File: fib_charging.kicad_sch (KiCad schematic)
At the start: 42 parts, among them J301 Conn_01x02, J302 Conn_01x02, J303 Conn_01x02, Q301 CSD17581Q3A, Q302 CSD17581Q3A, Q303 CSD17581Q3A, Q304 CSD17581Q3A, U301 BQ25798RQMR

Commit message: partially implemented E-INK PMIC
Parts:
- added R1, R2: 0R, Resistor_SMD:R_0603_1608Metric, symbol Device:R_Small
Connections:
- net USBPD1_HV: now also R1.2
- net USBPD2_HV: now also R2.2
- net VBUS_CHG: now also R1.1, R2.1
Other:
- note removed: "Can i just connect USBPD_HV-s together?"

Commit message: did a ton of routing and modeling for SOM, USB, DP & Charging/Power, things starting to take shape
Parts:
- J301, J302, J303: footprint Connector_JST:JST_EH_S2B-EH_1x02_P2.50mm_Horizontal -> Connector_JST:JST_PH_S2B-PH-SM4-TB_1x02-1MP_P2.00mm_Horizontal
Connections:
- net GND: now also J301.2 (Pin_2), J303.1 (Pin_1); no longer J301.1 (Pin_1), J303.2 (Pin_2)
- net CHG_VBUS: now reaches C303.1, C304.1, C307.1, Q303.5 (D), Q304.5 (D), U301.2 (VBUS), U301.3 (VBUS)
- net VBUS_SOLAR: now reaches C301.1, Q301.5 (D), U301.8 (VAC2)
- net VBUS_SOLAR: now also J301.1 (Pin_1); no longer J301.2 (Pin_2)
- net at C311.1, C314.1, R306.1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: now also J302.2 (Pin_2); no longer J302.1 (Pin_1)
- net VBUS_CHG renamed VBUS_USB
- new net: J302.1 (Pin_1), J303.2 (Pin_2)
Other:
- moved on the sheet: J301, J302, J303
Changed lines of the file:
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@@
 	(wire
 		(pts
-			(xy 222.25 104.14) (xy 227.33 104.14)
+			(xy 224.79 46.99) (xy 222.25 46.99)
 		)
 		(stroke
@@
 	(wire
 		(pts
-			(xy 199.39 91.44) (xy 199.39 93.98)
+			(xy 222.25 104.14) (xy 227.33 104.14)
 		)
 		(stroke
@@
 	(wire
 		(pts
-			(xy 120.65 55.88) (xy 130.81 55.88)
+			(xy 199.39 91.44) (xy 199.39 93.98)
 		)
 		(stroke
@@
 	(wire
 		(pts
-			(xy 81.28 82.55) (xy 87.63 82.55)
+			(xy 120.65 55.88) (xy 130.81 55.88)
 		)
 		(stroke
@@
 	(wire
 		(pts
-			(xy 224.79 60.96) (xy 224.79 64.77)
+			(xy 81.28 82.55) (xy 87.63 82.55)
 		)
 		(stroke
@@
 	(wire
 		(pts
+			(xy 45.72 68.58) (xy 48.26 68.58)
+		)
+		(stroke
+			(width 0)
+			(type default)
+		)
+	)
+	(wire
+		(pts
 			(xy 209.55 63.5) (xy 209.55 64.77)
 		)
@@
 	(wire
 		(pts
-			(xy 124.46 96.52) (xy 127 96.52)
+			(xy 222.25 46.99) (xy 222.25 52.07)
 		)
 		(stroke
@@
 	(wire
 		(pts
-			(xy 223.52 67.31) (xy 224.79 67.31)
+			(xy 124.46 96.52) (xy 127 96.52)
 		)
 		(stroke
@@
 	(wire
 		(pts
-			(xy 45.72 68.58) (xy 48.26 68.58)
+			(xy 45.72 66.04) (xy 53.34 66.04)
 		)
 		(stroke
@@
 	(wire
 		(pts
-			(xy 45.72 66.04) (xy 53.34 66.04)
+			(xy 187.96 90.17) (xy 187.96 91.44)
 		)
 		(stroke
@@
 	(wire
 		(pts
-			(xy 187.96 90.17) (xy 187.96 91.44)
+			(xy 189.23 58.42) (xy 189.23 60.96)
 		)
 		(stroke
@@
 	(wire
 		(pts
-			(xy 189.23 58.42) (xy 189.23 60.96)
+			(xy 87.63 63.5) (xy 102.87 63.5)
 		)
 		(stroke
@@
 	(wire
 		(pts
-			(xy 87.63 63.5) (xy 102.87 63.5)
+			(xy 224.79 49.53) (xy 224.79 55.88)
 		)
 		(stroke
@@
 		)
 	)
+	(label "VBUS_SOLAR"
+		(at 59.69 66.04 0)
+		(fields_autoplaced yes)
+		(effects
+			(font
+				(size 1.27 1.27)
+			)
+			(justify left bottom)
+		)
+	)
+	(label "CHG_VBUS"
+		(at 113.03 73.66 0)
+		(fields_autoplaced yes)
+		(effects
+			(font
+				(size 1.27 1.27)
+			)
+			(justify left bottom)
+		)
+	)
 	(global_label "~{CHG_CE}"
 		(shape input)
@@
 	(symbol
 		(lib_id "Connector_Generic:Conn_01x02")
-		(at 229.87 58.42 0)
+		(at 229.87 55.88 0)
 		(unit 1)
 		(exclude_from_sim no)
@@
 		(fields_autoplaced yes)
 		(property "Reference" "J302"
-			(at 232.41 58.4199 0)
+			(at 232.41 55.8799 0)
 			(effects
 				(font
@@
 		)
 		(property "Value" "Conn_01x02"
-			(at 232.41 60.9599 0)
+			(at 232.41 58.4199 0)
 			(effects
 				(font
@@
 			)
 		)
-		(property "Footprint" "Connector_JST:JST_EH_S2B-EH_1x02_P2.50mm_Horizontal"
-			(at 229.87 58.42 0)
+		(property "Footprint" "Connector_JST:JST_PH_S2B-PH-SM4-TB_1x02-1MP_P2.00mm_Horizontal"
+			(at 229.87 55.88 0)
 			(effects
 				(font
@@
 		)
 		(property "Datasheet" "~"
-			(at 229.87 58.42 0)
+			(at 229.87 55.88 0)
 			(effects
 				(font
@@
 		)
 		(property "Description" "Generic connector, single row, 01x02, script generated (kicad-library-utils/schlib/autogen/connector/)"
-			(at 229.87 58.42 0)
+			(at 229.87 55.88 0)
 			(effects
 				(font
@@
 	(symbol
 		(lib_id "Connector_Generic:Conn_01x02")
-		(at 229.87 64.77 0)
+		(at 229.87 46.99 0)
 		(unit 1)
 		(exclude_from_sim no)
@@
 		(fields_autoplaced yes)
 		(property "Reference" "J303"
-			(at 232.41 64.7699 0)
+			(at 232.41 46.9899 0)
 			(effects
 				(font
@@
 		)
 		(property "Value" "Conn_01x02"
-			(at 232.41 67.3099 0)
+			(at 232.41 49.5299 0)
 			(effects
 				(font
@@
 			)
 		)
-		(property "Footprint" "Connector_JST:JST_EH_S2B-EH_1x02_P2.50mm_Horizontal"
-			(at 229.87 64.77 0)
+		(property "Footprint" "Connector_JST:JST_PH_S2B-PH-SM4-TB_1x02-1MP_P2.00mm_Horizontal"
+			(at 229.87 46.99 0)
 			(effects
 				(font
@@
 		)
 		(property "Datasheet" "~"
-			(at 229.87 64.77 0)
+			(at 229.87 46.99 0)
 			(effects
 				(font
@@
 		)
 		(property "Description" "Generic connector, single row, 01x02, script generated (kicad-library-utils/schlib/autogen/connector/)"
-			(at 229.87 64.77 0)
+			(at 229.87 46.99 0)
 			(effects
 				(font
@@
 	(symbol
 		(lib_id "power:GND")
-		(at 223.52 67.31 0)
+		(at 222.25 52.07 0)
 		(unit 1)
 		(exclude_from_sim no)
@@
 		(fields_autoplaced yes)
 		(property "Reference" "#PWR0314"
-			(at 223.52 73.66 0)
+			(at 222.25 58.42 0)
 			(effects
 				(font
@@
 		)
 		(property "Value" "GND"
-			(at 223.52 72.39 0)
+			(at 222.25 57.15 0)
 			(effects
 				(font
@@
 		)
 		(property "Footprint" ""
-			(at 223.52 67.31 0)
+			(at 222.25 52.07 0)
 			(effects
 				(font
@@
 		)
 		(property "Datasheet" ""
-			(at 223.52 67.31 0)
+			(at 222.25 52.07 0)
 			(effects
 				(font
@@
 		)
 		(property "Description" "Power symbol creates a global label with name \"GND\" , ground"
-			(at 223.52 67.31 0)
+			(at 222.25 52.07 0)
 			(effects
 				(font
@@
 	(symbol
 		(lib_id "Connector_Generic:Conn_01x02")
-		(at 40.64 68.58 180)
+		(at 40.64 66.04 0)
+		(mirror y)
 		(unit 1)
 		(exclude_from_sim no)
@@
 		(on_board yes)
 		(dnp no)
-		(fields_autoplaced yes)
 		(property "Reference" "J301"
-			(at 40.64 59.69 0)
+			(at 40.64 74.93 0)
 			(effects
 				(font
@@
 		)
 		(property "Value" "Conn_01x02"
-			(at 40.64 62.23 0)
+			(at 40.64 72.39 0)
 			(effects
 				(font
@@
 			)
 		)
-		(property "Footprint" "Connector_JST:JST_EH_S2B-EH_1x02_P2.50mm_Horizontal"
-			(at 40.64 68.58 0)
+		(property "Footprint" "Connector_JST:JST_PH_S2B-PH-SM4-TB_1x02-1MP_P2.00mm_Horizontal"
+			(at 40.64 66.04 0)
 			(effects
 				(font
@@
 		)
 		(property "Datasheet" "~"
-			(at 40.64 68.58 0)
+			(at 40.64 66.04 0)
 			(effects
 				(font
@@
 		)
 		(property "Description" "Generic connector, single row, 01x02, script generated (kicad-library-utils/schlib/autogen/connector/)"
-			(at 40.64 68.58 0)
+			(at 40.64 66.04 0)
 			(effects
 				(font
@@
 			)
 		)
-		(property "Value" "VBUS_CHG"
+		(property "Value" "VBUS_USB"
 			(at 66.04 69.85 0)
 			(effects
@@
 			)
 		)
-		(property "Value" "VBUS_CHG"
+		(property "Value" "VBUS_USB"
 			(at 55.88 91.44 0)
 			(effects

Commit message: implemented most of USB and Power Supplies
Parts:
- added C30, C31: 10uF, Capacitor_SMD:C_0603_1608Metric, symbol Device:C_Small
- C301, C302, C303, C305, C306, C309, C310: footprint Capacitor_SMD:C_0603_1608Metric -> Capacitor_SMD:C_0402_1005Metric
- D303: footprint Capacitor_SMD:C_0603_1608Metric -> (none)
- L301: footprint Resistor_SMD:R_0603_1608Metric -> (none)
- R301, R302, R303, R304, R305, R306, R307, R308, R309, TH301: footprint Resistor_SMD:R_0603_1608Metric -> Resistor_SMD:R_0402_1005Metric
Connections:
- net GND: now also C30.2, C31.2
- net VBUS_SOLAR: now also C30.1
- net VBUS_USB: now also C31.1

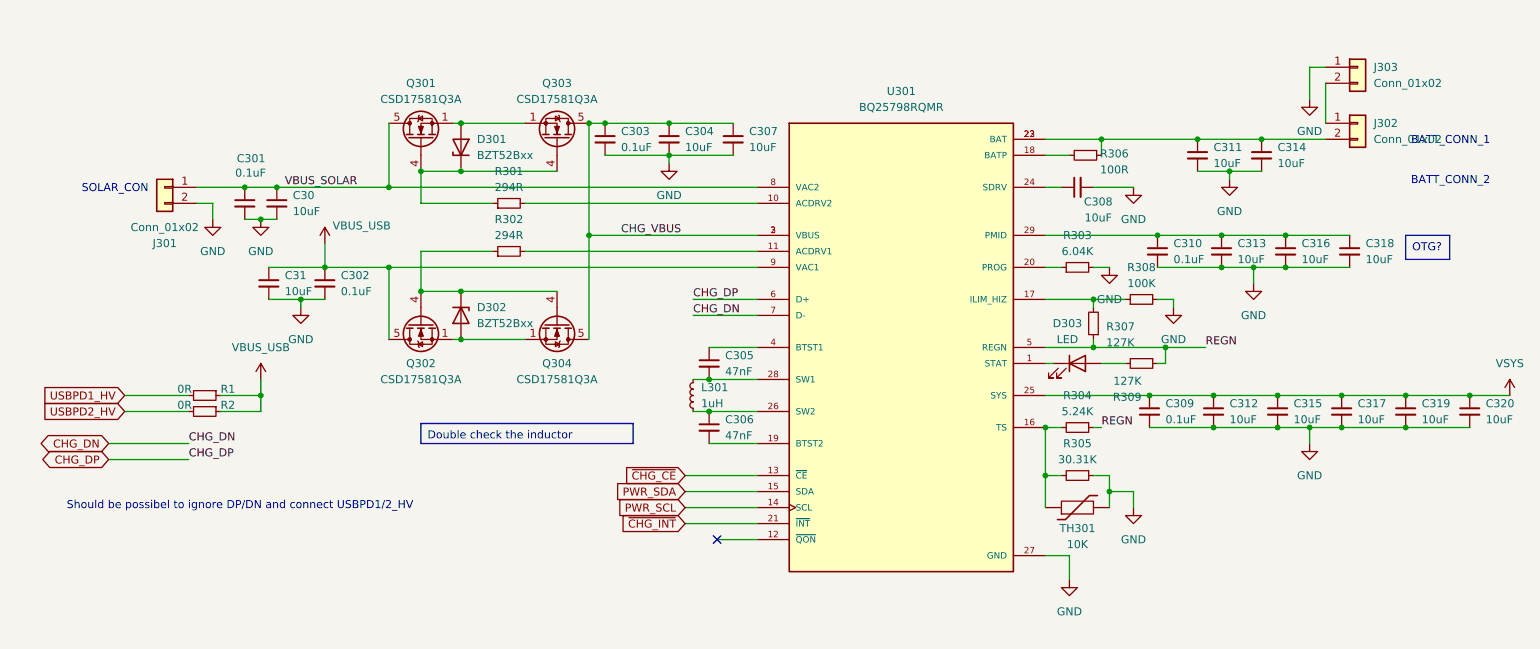
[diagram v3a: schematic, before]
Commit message: further optimized placement, finished most of buck array, expanded pcie, added tons of missing footprints, diff pair spacing optimization
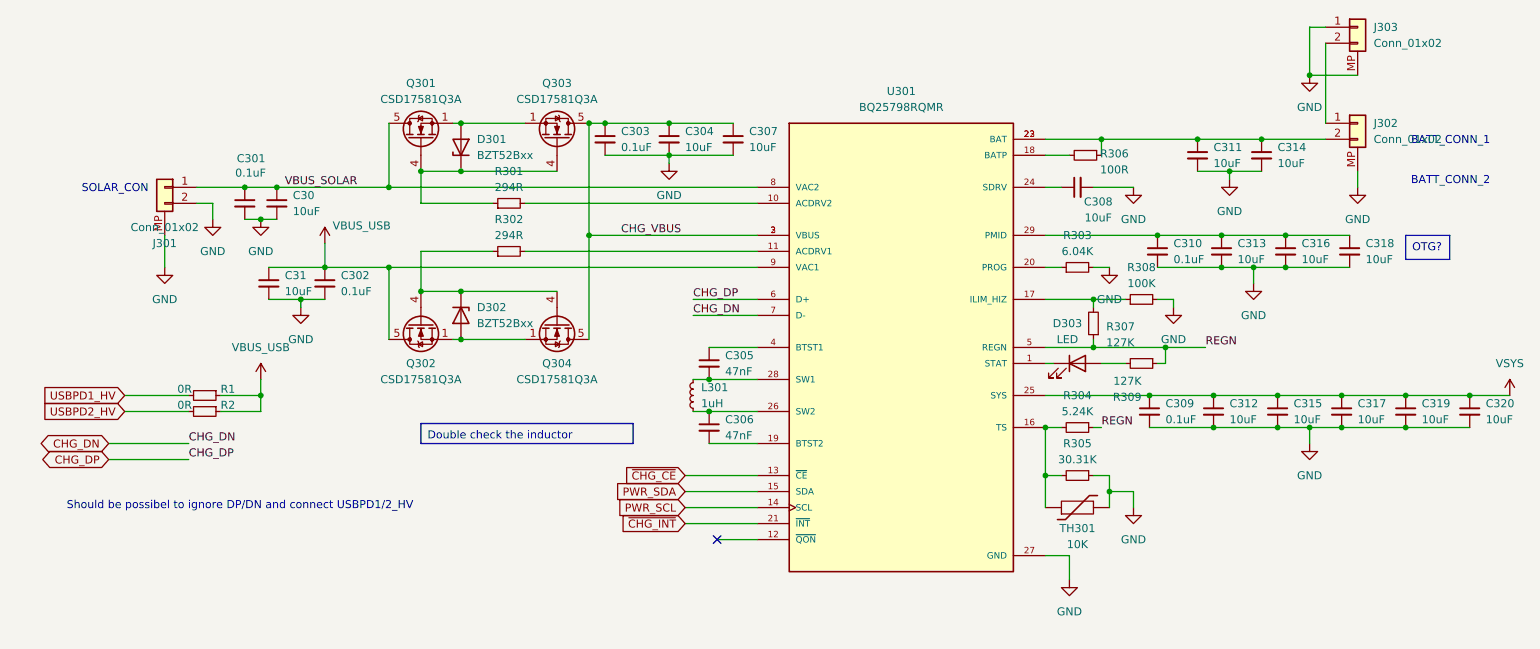
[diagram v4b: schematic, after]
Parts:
- D303: footprint (none) -> LED_SMD:LED_0603_1608Metric
- J301, J302, J303: symbol Connector_Generic:Conn_01x02 -> Fibel2:JST_2_SMD
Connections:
- net GND: now also J301.MP, J302.MP, J303.MP
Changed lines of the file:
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@@
 		(color 0 0 0 0)
 	)
+	(junction
+		(at 222.25 48.26)
+		(diameter 0)
+		(color 0 0 0 0)
+	)
 	(no_connect
 		(at 128.27 121.92)
@@
 	(wire
 		(pts
-			(xy 224.79 46.99) (xy 222.25 46.99)
+			(xy 224.79 40.64) (xy 222.25 40.64)
 		)
 		(stroke
@@
 	(wire
 		(pts
-			(xy 222.25 46.99) (xy 222.25 52.07)
+			(xy 40.64 78.74) (xy 40.64 73.66)
+		)
+		(stroke
+			(width 0)
+			(type default)
+		)
+	)
+	(wire
+		(pts
+			(xy 222.25 40.64) (xy 222.25 48.26)
 		)
 		(stroke
@@
 	(wire
 		(pts
+			(xy 222.25 48.26) (xy 229.87 48.26)
+		)
+		(stroke
+			(width 0)
+			(type default)
+		)
+	)
+	(wire
+		(pts
 			(xy 81.28 76.2) (xy 81.28 82.55)
 		)
@@
 	(wire
 		(pts
+			(xy 229.87 63.5) (xy 229.87 66.04)
+		)
+		(stroke
+			(width 0)
+			(type default)
+		)
+	)
+	(wire
+		(pts
 			(xy 237.49 99.06) (xy 247.65 99.06)
 		)
@@
 	(wire
 		(pts
-			(xy 224.79 49.53) (xy 224.79 55.88)
+			(xy 224.79 43.18) (xy 224.79 55.88)
 		)
 		(stroke
@@
 	)
 	(symbol
+		(lib_id "power:GND")
+		(at 40.64 78.74 0)
+		(unit 1)
+		(exclude_from_sim no)
+		(in_bom yes)
+		(on_board yes)
+		(dnp no)
+		(fields_autoplaced yes)
+		(property "Reference" "#PWR036"
+			(at 40.64 85.09 0)
+			(effects
+				(font
+					(size 1.27 1.27)
+				)
+				(hide yes)
+			)
+		)
+		(property "Value" "GND"
+			(at 40.64 83.82 0)
+			(effects
+				(font
+					(size 1.27 1.27)
+				)
+			)
+		)
+		(property "Footprint" ""
+			(at 40.64 78.74 0)
+			(effects
+				(font
+					(size 1.27 1.27)
+				)
+				(hide yes)
+			)
+		)
+		(property "Datasheet" ""
+			(at 40.64 78.74 0)
+			(effects
+				(font
+					(size 1.27 1.27)
+				)
+				(hide yes)
+			)
+		)
+		(property "Description" "Power symbol creates a global label with name \"GND\" , ground"
+			(at 40.64 78.74 0)
+			(effects
+				(font
+					(size 1.27 1.27)
+				)
+				(hide yes)
+			)
+		)
+		(pin "1"
+		)
+		(instances
+			(project "Fibel2"
+				(path "/862c21e2-7ec9-4f80-a33c-aad02ea9423e/23d4f4f3-5c09-4966-9bf4-edbe4cd81212"
+					(reference "#PWR036")
+					(unit 1)
+				)
+			)
+		)
+	)
+	(symbol
 		(lib_id "Device:C_Small")
 		(at 185.42 66.04 90)
@@
 	)
 	(symbol
-		(lib_id "Connector_Generic:Conn_01x02")
+		(lib_id "Fibel2:JST_2_SMD")
 		(at 229.87 55.88 0)
 		(unit 1)
@@
 		(pin "2"
 		)
+		(pin "MP"
+		)
 		(instances
 			(project "Fibel2"
@@
 	)
 	(symbol
-		(lib_id "Connector_Generic:Conn_01x02")
-		(at 229.87 46.99 0)
+		(lib_id "Fibel2:JST_2_SMD")
+		(at 229.87 40.64 0)
 		(unit 1)
 		(exclude_from_sim no)
@@
 		(fields_autoplaced yes)
 		(property "Reference" "J303"
-			(at 232.41 46.9899 0)
+			(at 232.41 40.6399 0)
 			(effects
 				(font
@@
 		)
 		(property "Value" "Conn_01x02"
-			(at 232.41 49.5299 0)
+			(at 232.41 43.1799 0)
 			(effects
 				(font
@@
 		)
 		(property "Footprint" "Connector_JST:JST_PH_S2B-PH-SM4-TB_1x02-1MP_P2.00mm_Horizontal"
-			(at 229.87 46.99 0)
+			(at 229.87 40.64 0)
 			(effects
 				(font
@@
 		)
 		(property "Datasheet" "~"
-			(at 229.87 46.99 0)
+			(at 229.87 40.64 0)
 			(effects
 				(font
@@
 		)
 		(property "Description" "Generic connector, single row, 01x02, script generated (kicad-library-utils/schlib/autogen/connector/)"
-			(at 229.87 46.99 0)
+			(at 229.87 40.64 0)
 			(effects
 				(font
@@
 		(pin "2"
 		)
+		(pin "MP"
+		)
 		(instances
 			(project "Fibel2"
@@
 	(symbol
 		(lib_id "power:GND")
-		(at 222.25 52.07 0)
+		(at 222.25 48.26 0)
 		(unit 1)
 		(exclude_from_sim no)
@@
 		(fields_autoplaced yes)
 		(property "Reference" "#PWR0314"
-			(at 222.25 58.42 0)
+			(at 222.25 54.61 0)
 			(effects
 				(font
@@
 		)
 		(property "Value" "GND"
-			(at 222.25 57.15 0)
+			(at 222.25 53.34 0)
 			(effects
 				(font
@@
 		)
 		(property "Footprint" ""
-			(at 222.25 52.07 0)
+			(at 222.25 48.26 0)
 			(effects
 				(font
@@
 		)
 		(property "Datasheet" ""
-			(at 222.25 52.07 0)
+			(at 222.25 48.26 0)
 			(effects
 				(font
@@
 		)
 		(property "Description" "Power symbol creates a global label with name \"GND\" , ground"
-			(at 222.25 52.07 0)
+			(at 222.25 48.26 0)
 			(effects
 				(font
@@
 	)
 	(symbol
-		(lib_id "Connector_Generic:Conn_01x02")
+		(lib_id "Fibel2:JST_2_SMD")
 		(at 40.64 66.04 0)
 		(mirror y)
@@
 		(pin "2"
 		)
+		(pin "MP"
+		)
 		(instances
 			(project "Fibel2"
@@
 			)
 		)
-		(property "Footprint" ""
+		(property "Footprint" "LED_SMD:LED_0603_1608Metric"
 			(at 185.42 93.98 0)
 			(effects
@@
 					(unit 1)
 				)
+			)
+		)
+	)
+	(symbol
+		(lib_id "power:GND")
+		(at 229.87 66.04 0)
+		(unit 1)
+		(exclude_from_sim no)
+		(in_bom yes)
+		(on_board yes)
+		(dnp no)
+		(fields_autoplaced yes)
+		(property "Reference" "#PWR035"
+			(at 229.87 72.39 0)
+			(effects
+				(font
+					(size 1.27 1.27)
+				)
+				(hide yes)
+			)
+		)
+		(property "Value" "GND"
+			(at 229.87 71.12 0)
+			(effects
+				(font
+					(size 1.27 1.27)
+				)
+			)
+		)
+		(property "Footprint" ""
+			(at 229.87 66.04 0)
+			(effects
+				(font
+					(size 1.27 1.27)
+				)
+				(hide yes)
+			)
+		)
+		(property "Datasheet" ""
+			(at 229.87 66.04 0)
+			(effects
+				(font
+					(size 1.27 1.27)
+				)
+				(hide yes)
+			)
+		)
+		(property "Description" "Power symbol creates a global label with name \"GND\" , ground"
+			(at 229.87 66.04 0)
+			(effects
+				(font
+					(size 1.27 1.27)
+				)
+				(hide yes)
+			)
+		)
+		(pin "1"
+		)
+		(instances
+			(project "Fibel2"
+				(path "/862c21e2-7ec9-4f80-a33c-aad02ea9423e/23d4f4f3-5c09-4966-9bf4-edbe4cd81212"
+					(reference "#PWR035")
+					(unit 1)
+				)

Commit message: 90 percent done with routing. need to go over all schematic pages, double check everything thoroughly, do lengthmatching add any missing footprints, take care of startup, ferrites, audio, eink connectors, 40pin header connections, rtc
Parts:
- L301: footprint (none) -> Fibel2:SPM6530
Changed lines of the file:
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@@
 			)
 		)
-		(property "Footprint" ""
+		(property "Footprint" "Fibel2:SPM6530"
 			(at 124.46 99.06 0)
 			(effects

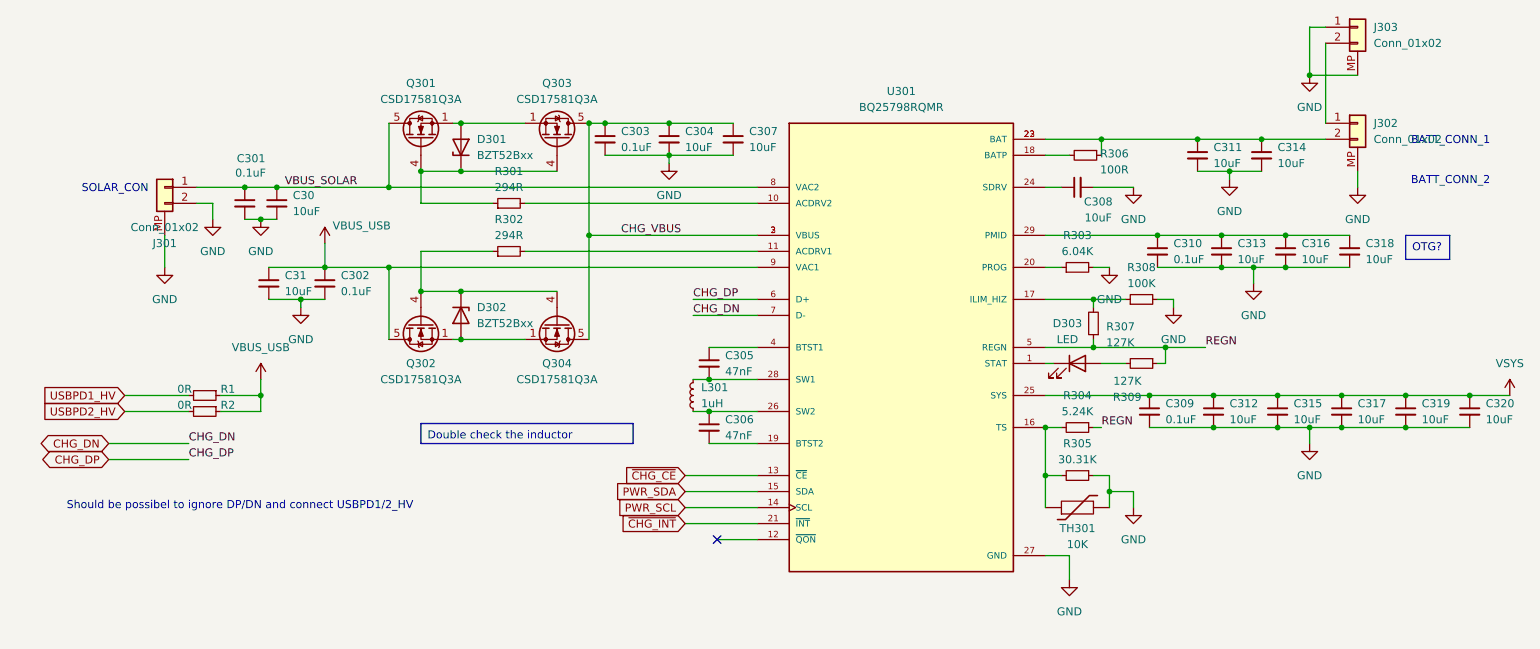
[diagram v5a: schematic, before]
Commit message: routed epd displays, added testpoints and all the little checks and fixe, (regrettably) removed the i80 connector, 99% there, need to double check some things add peripheral connectors, shared-ish storage and vias vias vias
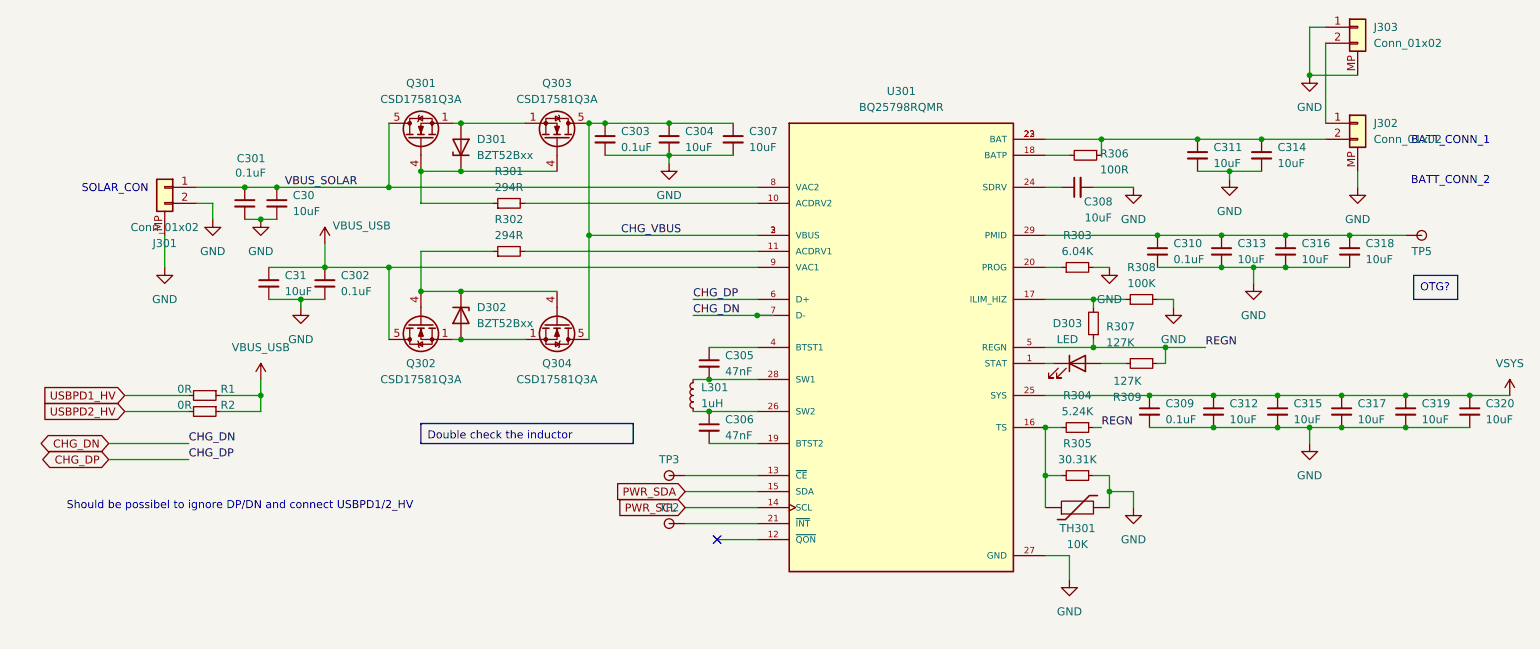
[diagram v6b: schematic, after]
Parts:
- added TP2, TP3, TP5: TestPoint, TestPoint:TestPoint_Pad_D1.0mm, symbol Fibel2:TestPoint
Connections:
- net at C310.1, C313.1, C316.1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: now also TP5.1
- net ~{CHG_CE}: no longer names the net of U301.13 (~{CE})
- net ~{CHG_CE}: now also TP3.1
- net ~{CHG_INT}: no longer names the net of U301.21 (~{INT})
- net ~{CHG_INT}: now also TP2.1
